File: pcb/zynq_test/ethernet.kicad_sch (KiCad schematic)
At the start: 62 parts, among them J1101 RJ45_JK0654219, Q1101 FDY102PZ, Q1102 NMOS, Q1103 NMOS, U1101 LAN8830, U1102 DSC1001CI2-025

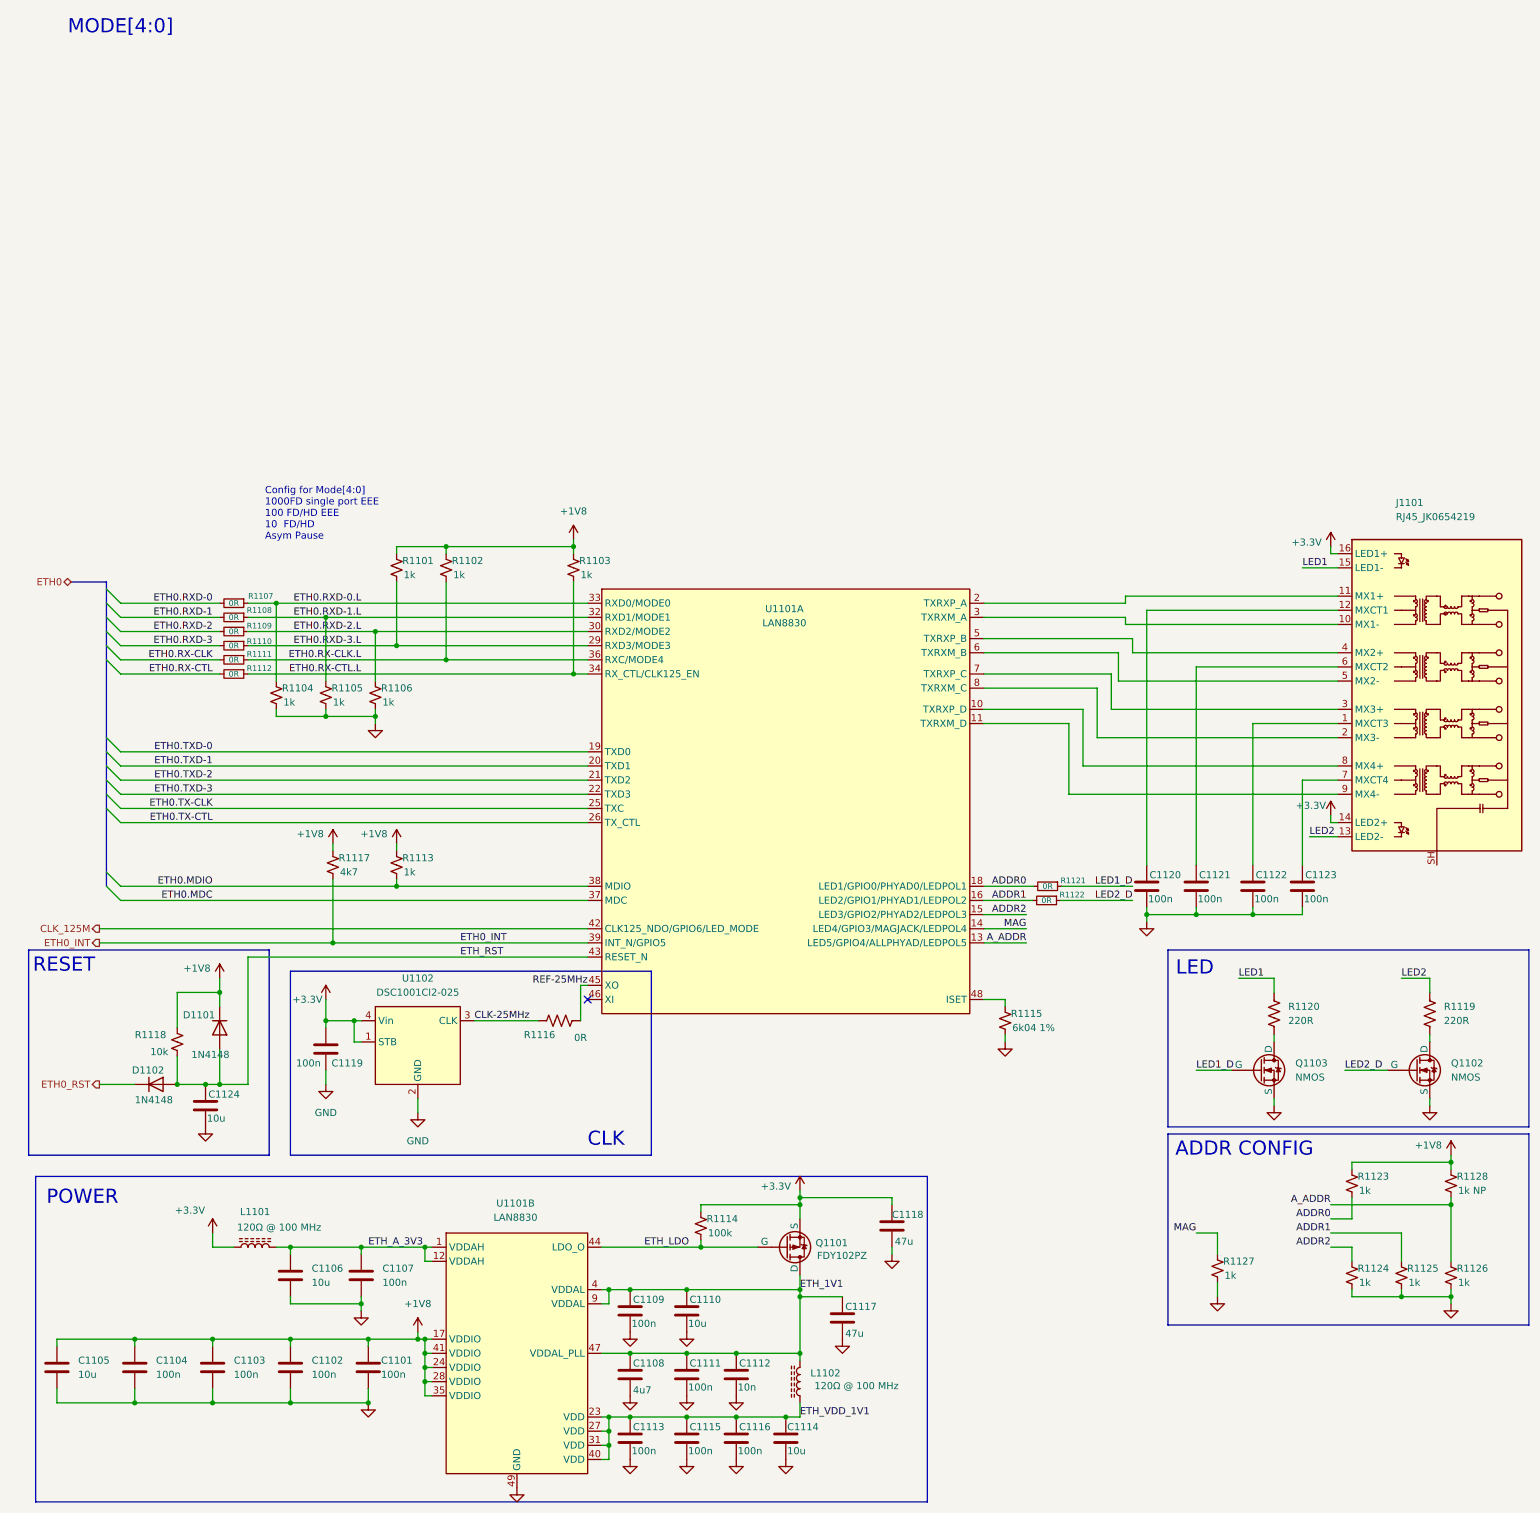
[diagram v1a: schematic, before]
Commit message: Finished HDMI
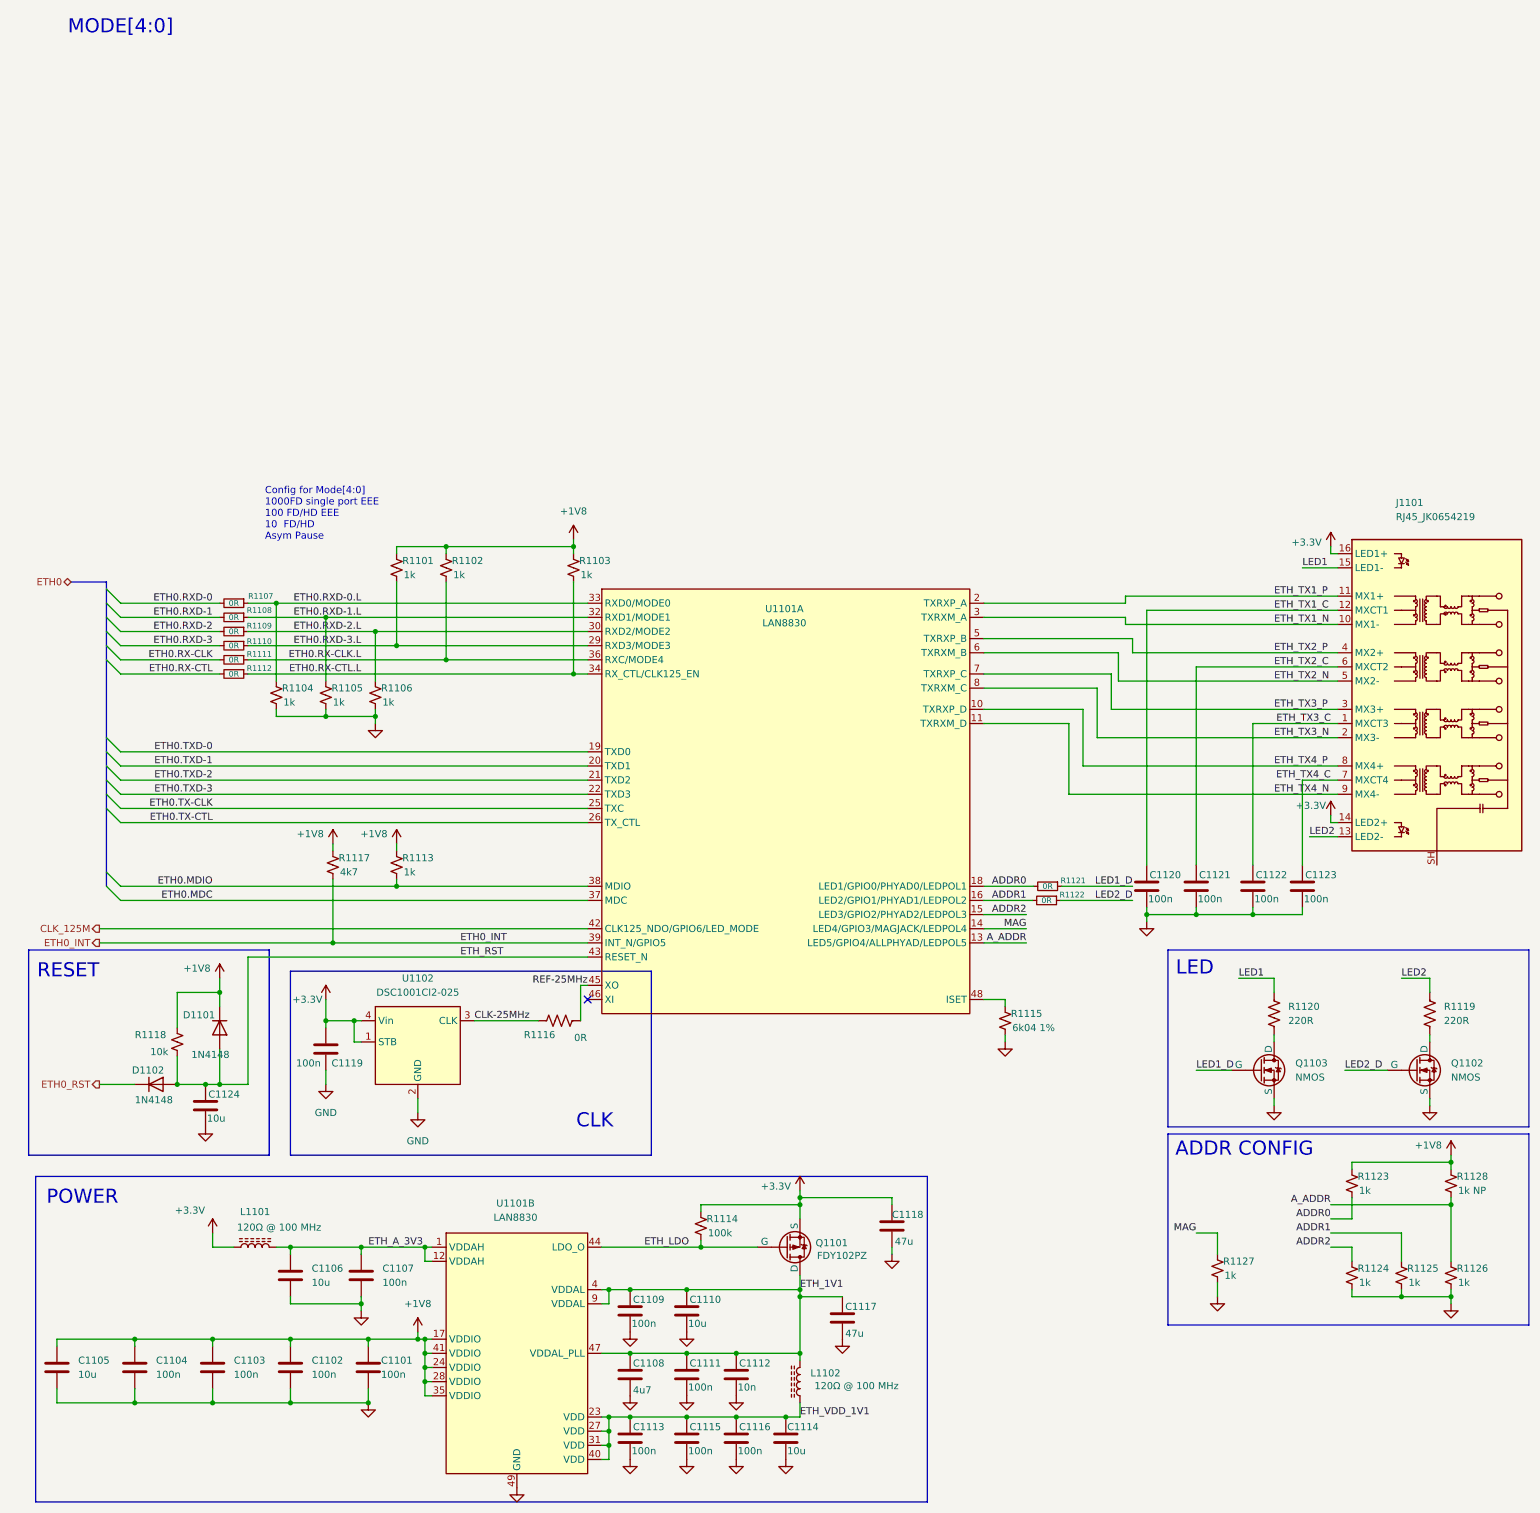
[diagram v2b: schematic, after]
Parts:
- U1101: footprint (none) -> Package_DFN_QFN:VQFN-48-1EP_7x7mm_P0.5mm_EP4.1x4.1mm
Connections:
- net ETH_TX3_C: now reaches C1122.1, J1101.1 (MXCT3)
- net ETH_TX4_C: now reaches C1123.1, J1101.7 (MXCT4)
- net ETH_TX1_C: now reaches C1120.1, J1101.12 (MXCT1)
- net ETH_TX4_P: now reaches J1101.8 (MX4+), U1101.10 (TXRXP_D)
- net ETH_TX4_N: now reaches J1101.9 (MX4-), U1101.11 (TXRXM_D)
- net ETH_TX1_P: now reaches J1101.11 (MX1+), U1101.2 (TXRXP_A)
- net ETH_TX1_N: now reaches J1101.10 (MX1-), U1101.3 (TXRXM_A)
- net ETH_TX2_P: now reaches J1101.4 (MX2+), U1101.5 (TXRXP_B)
- net ETH_TX2_N: now reaches J1101.5 (MX2-), U1101.6 (TXRXM_B)
- net ETH_TX3_P: now reaches J1101.3 (MX3+), U1101.7 (TXRXP_C)
- net ETH_TX3_N: now reaches J1101.2 (MX3-), U1101.8 (TXRXM_C)
- net ETH_TX2_C: now reaches C1121.1, J1101.6 (MXCT2)
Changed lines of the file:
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@@
 	(text "RESET"
 		(exclude_from_sim no)
-		(at 21.59 100.584 0)
+		(at 22.352 101.6 0)
 		(effects
 			(font
@@
 	(text "CLK"
 		(exclude_from_sim no)
-		(at 118.872 131.826 0)
+		(at 116.84 128.524 0)
 		(effects
 			(font
@@
 		)
 	)
+	(label "ETH_TX2_P"
+		(at 238.76 44.45 0)
+		(effects
+			(font
+				(size 1.27 1.27)
+			)
+			(justify left bottom)
+		)
+	)
+	(label "ETH_TX2_C"
+		(at 238.76 46.99 0)
+		(effects
+			(font
+				(size 1.27 1.27)
+			)
+			(justify left bottom)
+		)
+	)
 	(label "A_ADDR"
 		(at 248.92 143.51 180)
@@
 		)
 	)
+	(label "ETH_TX1_P"
+		(at 238.76 34.29 0)
+		(effects
+			(font
+				(size 1.27 1.27)
+			)
+			(justify left bottom)
+		)
+	)
 	(label "ETH0.RXD-0.L"
 		(at 74.93 35.56 180)
@@
 		)
 	)
+	(label "ETH_TX2_N"
+		(at 238.76 49.53 0)
+		(effects
+			(font
+				(size 1.27 1.27)
+			)
+			(justify left bottom)
+		)
+	)
 	(label "LED1_D"
 		(at 224.79 119.38 0)
@@
 		)
 	)
+	(label "ETH_TX4_C"
+		(at 248.92 67.31 180)
+		(effects
+			(font
+				(size 1.27 1.27)
+			)
+			(justify right bottom)
+		)
+	)
+	(label "ETH_TX3_N"
+		(at 238.76 59.69 0)
+		(effects
+			(font
+				(size 1.27 1.27)
+			)
+			(justify left bottom)
+		)
+	)
 	(label "LED2_D"
 		(at 251.46 119.38 0)
@@
 		)
 	)
+	(label "ETH_TX4_P"
+		(at 238.76 64.77 0)
+		(effects
+			(font
+				(size 1.27 1.27)
+			)
+			(justify left bottom)
+		)
+	)
 	(label "ADDR0"
 		(at 194.31 86.36 180)
@@
 		)
 	)
+	(label "ETH_TX4_N"
+		(at 238.76 69.85 0)
+		(effects
+			(font
+				(size 1.27 1.27)
+			)
+			(justify left bottom)
+		)
+	)
 	(label "ETH0.TXD-3"
 		(at 48.26 69.85 180)
@@
 		)
 	)
+	(label "ETH_TX1_N"
+		(at 238.76 39.37 0)
+		(effects
+			(font
+				(size 1.27 1.27)
+			)
+			(justify left bottom)
+		)
+	)
+	(label "ETH_TX3_C"
+		(at 239.1554 57.15 0)
+		(effects
+			(font
+				(size 1.27 1.27)
+			)
+			(justify left bottom)
+		)
+	)
 	(label "ADDR0"
 		(at 248.92 146.05 180)
@@
 		)
 	)
+	(label "ETH_TX3_P"
+		(at 238.76 54.61 0)
+		(effects
+			(font
+				(size 1.27 1.27)
+			)
+			(justify left bottom)
+		)
+	)
 	(label "ETH_RST"
 		(at 92.71 99.06 0)
@@
 		)
 	)
+	(label "ETH_TX1_C"
+		(at 238.76 36.83 0)
+		(effects
+			(font
+				(size 1.27 1.27)
+			)
+			(justify left bottom)
+		)
+	)
 	(label "ETH0.RXD-0"
 		(at 48.26 35.56 180)
@@
 			)
 		)
-		(property "Footprint" ""
+		(property "Footprint" "Package_DFN_QFN:VQFN-48-1EP_7x7mm_P0.5mm_EP4.1x4.1mm"
 			(at 151.13 41.91 0)
 			(effects
@@
 			)
 		)
-		(property "Footprint" ""
+		(property "Footprint" "Package_DFN_QFN:VQFN-48-1EP_7x7mm_P0.5mm_EP4.1x4.1mm"
 			(at 102.87 148.59 0)
 			(effects

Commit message: Connected DDR3, cleaned up some thing
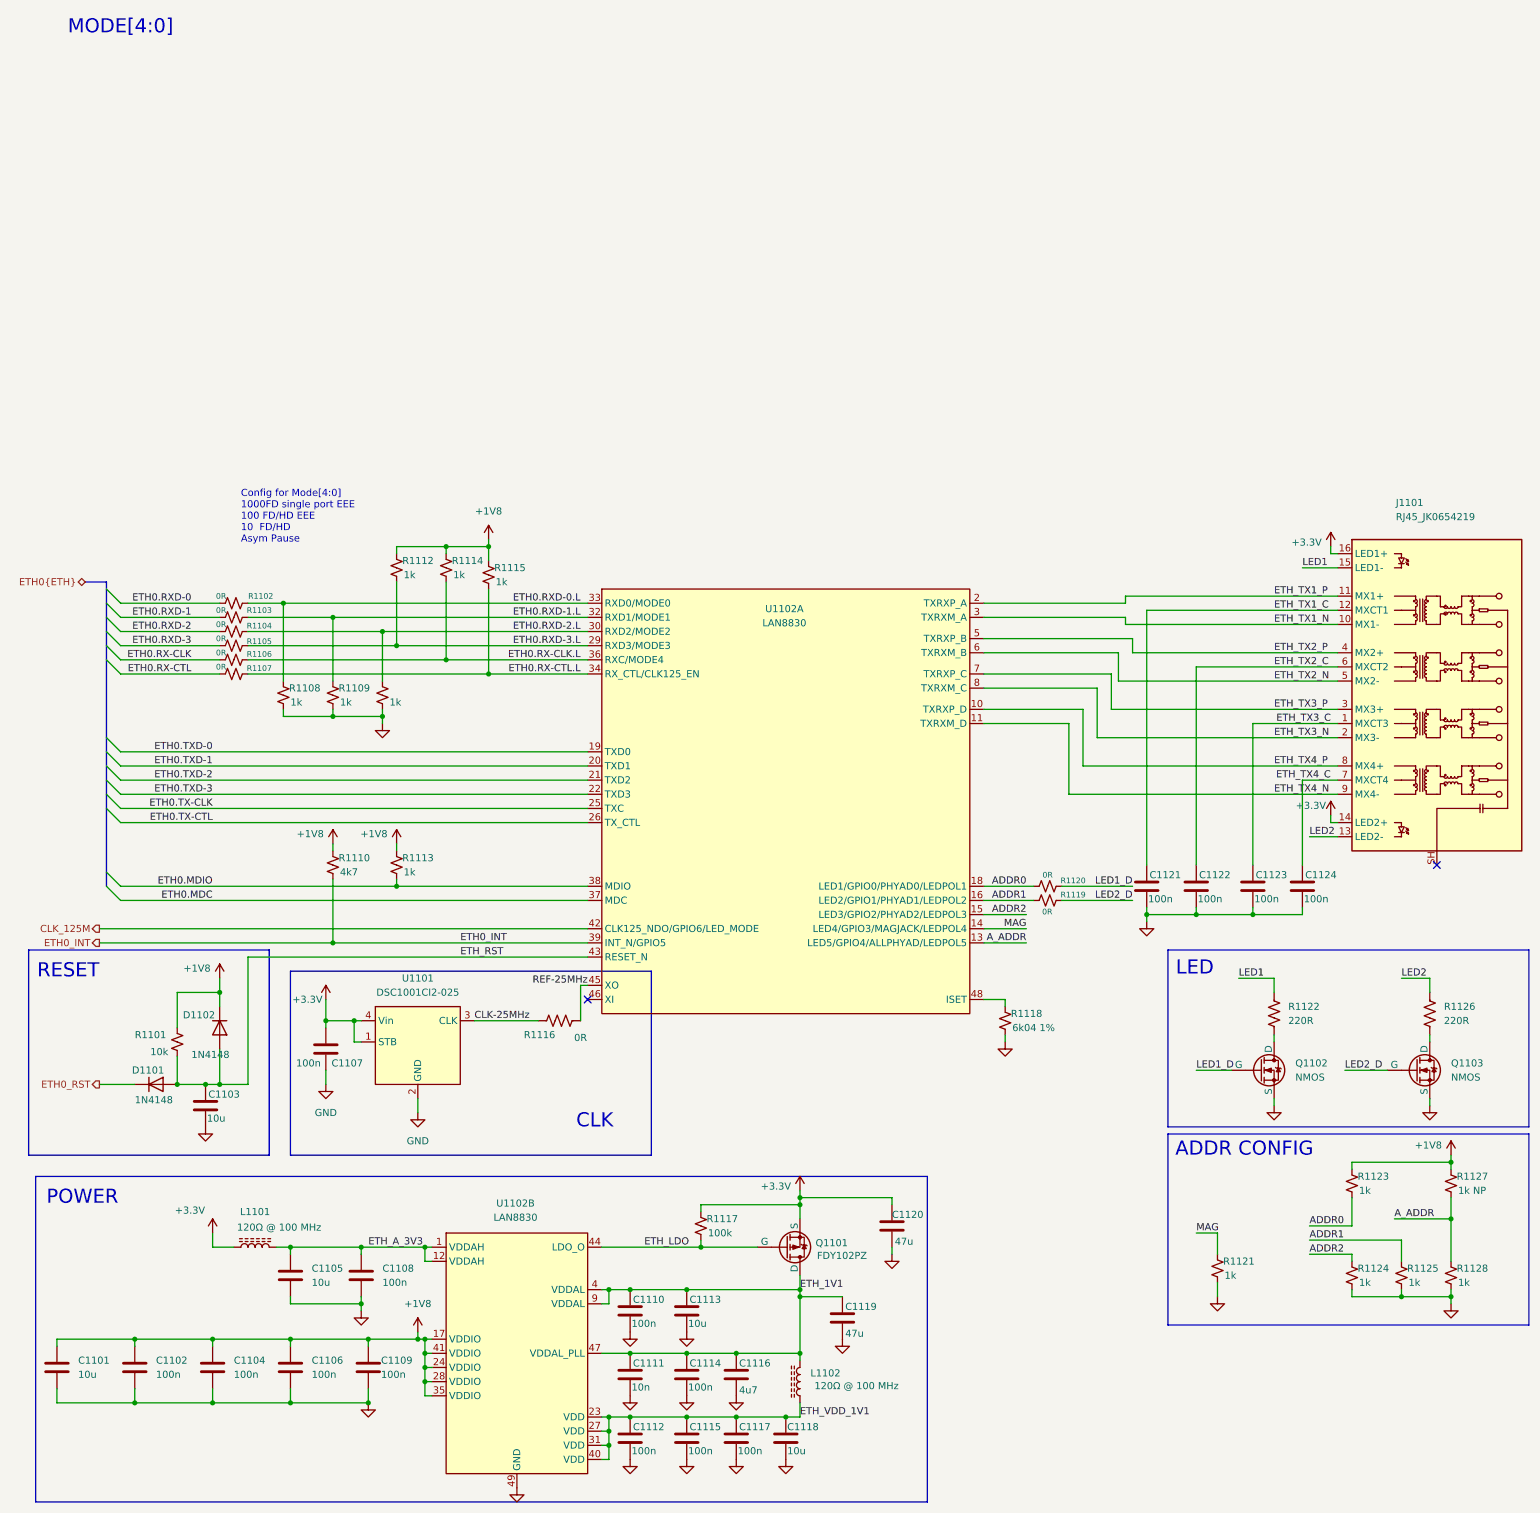
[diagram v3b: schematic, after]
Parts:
- R1102: renamed from R1107; symbol Device:R_Small -> Device:R_Small_US
- R1103: renamed from R1108; symbol Device:R_Small -> Device:R_Small_US
- R1104: renamed from R1109; symbol Device:R_Small -> Device:R_Small_US
- R1105: renamed from R1110; symbol Device:R_Small -> Device:R_Small_US
- R1106: renamed from R1111; symbol Device:R_Small -> Device:R_Small_US
- R1107: renamed from R1112; symbol Device:R_Small -> Device:R_Small_US
- R1119: renamed from R1122; symbol Device:R_Small -> Device:R_Small_US
- R1120: renamed from R1121; symbol Device:R_Small -> Device:R_Small_US
- renumbered C1105 to C1101, C1104 to C1102, C1124 to C1103, C1103 to C1104, C1106 to C1105, C1102 to C1106, C1119 to C1107, C1107 to C1108, C1101 to C1109, C1109 to C1110, C1112 to C1111, C1113 to C1112, C1110 to C1113, C1111 to C1114, C1108 to C1116, C1116 to C1117, C1114 to C1118, C1117 to C1119, C1118 to C1120, C1120 to C1121, C1121 to C1122, C1122 to C1123, C1123 to C1124, D1102 to D1101, D1101 to D1102, Q1103 to Q1102, Q1102 to Q1103, R1118 to R1101, R1104 to R1108, R1105 to R1109, R1117 to R1110, R1106 to R1111, R1101 to R1112, R1102 to R1114, R1103 to R1115, R1114 to R1117, R1115 to R1118, R1127 to R1121, R1120 to R1122, R1119 to R1126, R1128 to R1127, R1126 to R1128, U1102 to U1101, U1101 to U1102
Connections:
- net +3.3V: now also Q1101.3 (S); no longer Q1101.2 (S)
- net ETH_1V1: now also Q1101.1 (D); no longer Q1101.3 (D)
- net ETH_LDO: now also Q1101.2 (G); no longer Q1101.1 (G)
- no-connect marks 1 -> 2
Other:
- moved on the sheet: C1111, C1116, R1108, R1109, R1115
